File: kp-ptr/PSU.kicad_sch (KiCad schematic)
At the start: 34 parts, among them IC1 TPS62140ARGTR, J2 Conn_01x02, J3 Conn_01x02, U10 AZ1117CH-5.0TRG1, U9 LDFM33PVR

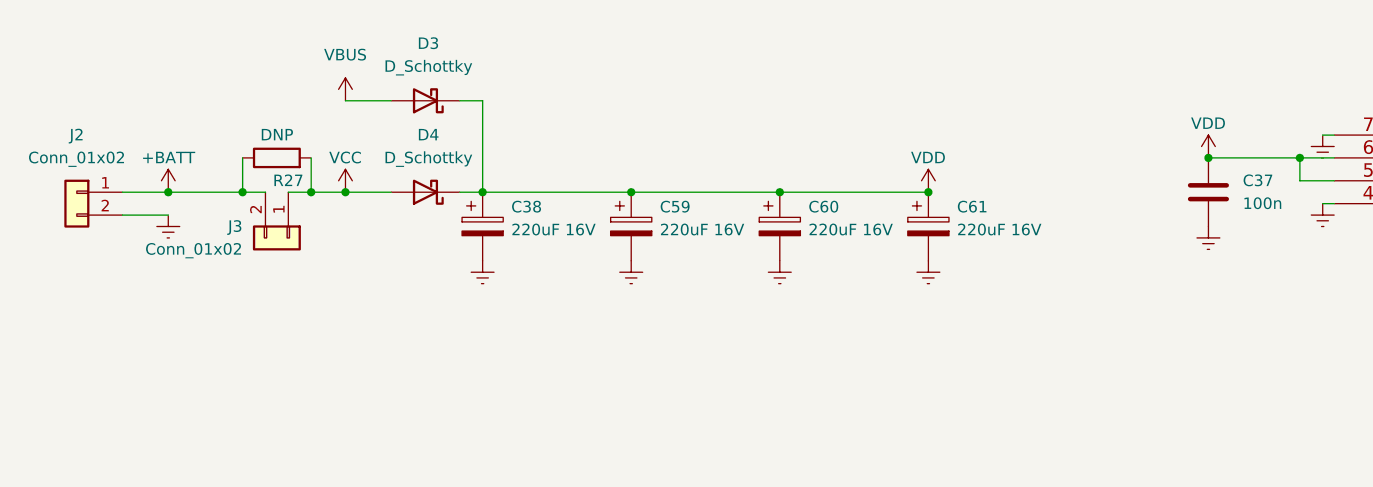
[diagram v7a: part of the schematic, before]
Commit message: SW removed, tantal added, powerplane rework
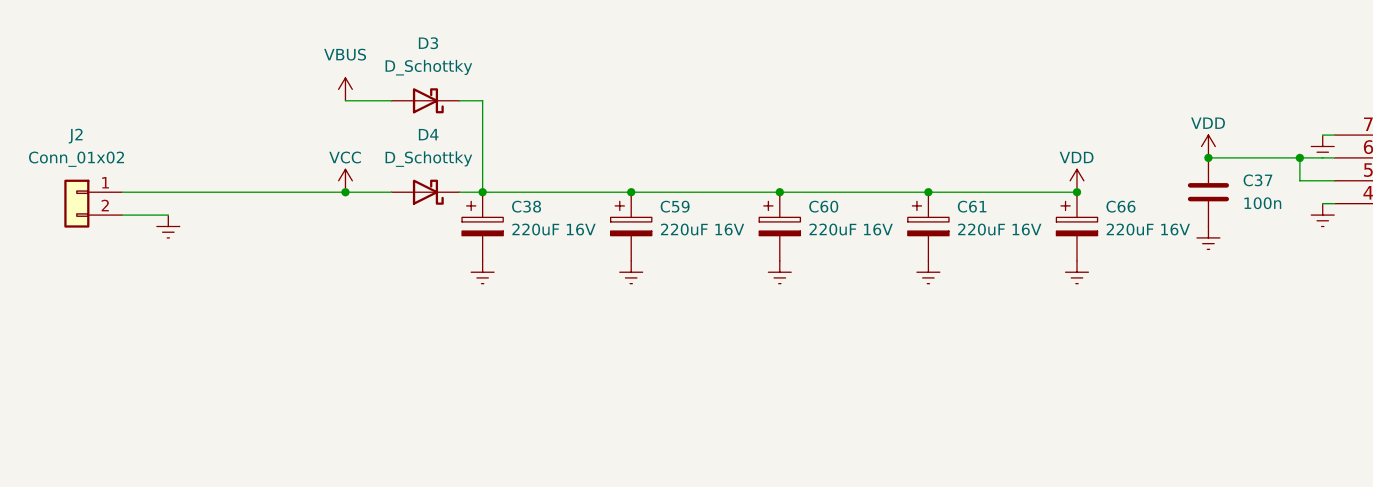
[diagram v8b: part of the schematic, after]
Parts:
- removed J3: Conn_01x02, TerminalBlock_TE-Connectivity:TerminalBlock_TE_282834-2_1x02_P2.54mm_Horizontal, symbol Connector_Generic:Conn_01x02
- removed R27: DNP, Resistor_SMD:R_1206_3216Metric, symbol Device:R
- added C66: 220uF 16V, Capacitor_Tantalum_SMD:CP_EIA-7343-31_Kemet-D, symbol Device:C_Polarized
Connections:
- net +BATT is gone; now on net VCC: J2.1 (Pin_1)
- net Earth: now also C66.2
- net VDD: now also C66.1
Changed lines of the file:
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@@
   (junction (at 41.275 97.79) (diameter 0) (color 0 0 0 0)
   )
-  (junction (at 47.625 44.45) (diameter 0) (color 0 0 0 0)
-  )
   (junction (at 149.86 129.54) (diameter 0) (color 0 0 0 0)
   )
@@
   (junction (at 147.32 40.64) (diameter 0) (color 0 0 0 0)
   )
-  (junction (at 31.75 44.45) (diameter 0) (color 0 0 0 0)
-  )
   (junction (at 137.16 132.08) (diameter 0) (color 0 0 0 0)
   )
   (junction (at 106.68 133.35) (diameter 0) (color 0 0 0 0)
   )
+  (junction (at 132.715 44.45) (diameter 0) (color 0 0 0 0)
+  )
   (junction (at 214.63 38.1) (diameter 0) (color 0 0 0 0)
-  )
-  (junction (at 40.005 44.45) (diameter 0) (color 0 0 0 0)
   )
   (junction (at 99.695 44.45) (diameter 0) (color 0 0 0 0)
@@
     (stroke (width 0) (type default) (color 0 0 0 0))
   )
-  (wire (pts (xy 45.085 44.45) (xy 47.625 44.45))
-    (stroke (width 0) (type default) (color 0 0 0 0))
-  )
   (wire (pts (xy 99.695 44.45) (xy 116.205 44.45))
     (stroke (width 0) (type default) (color 0 0 0 0))
@@
     (stroke (width 0) (type default) (color 0 0 0 0))
   )
-  (wire (pts (xy 47.625 40.64) (xy 47.625 44.45))
-    (stroke (width 0) (type default) (color 0 0 0 0))
-  )
   (wire (pts (xy 144.78 144.78) (xy 149.86 144.78))
     (stroke (width 0) (type default) (color 0 0 0 0))
@@
     (stroke (width 0) (type default) (color 0 0 0 0))
   )
-  (wire (pts (xy 47.625 44.45) (xy 51.435 44.45))
-    (stroke (width 0) (type default) (color 0 0 0 0))
-  )
-  (wire (pts (xy 26.67 44.45) (xy 31.75 44.45))
+  (wire (pts (xy 26.67 44.45) (xy 51.435 44.45))
+    (stroke (width 0) (type default) (color 0 0 0 0))
+  )
+  (wire (pts (xy 116.205 44.45) (xy 132.715 44.45))
     (stroke (width 0) (type default) (color 0 0 0 0))
   )
@@
     (stroke (width 0) (type default) (color 0 0 0 0))
   )
-  (wire (pts (xy 31.75 44.45) (xy 40.005 44.45))
-    (stroke (width 0) (type default) (color 0 0 0 0))
-  )
   (wire (pts (xy 160.02 38.1) (xy 161.29 38.1))
     (stroke (width 0) (type default) (color 0 0 0 0))
@@
     (stroke (width 0) (type default) (color 0 0 0 0))
   )
-  (wire (pts (xy 40.005 40.64) (xy 40.005 44.45))
-    (stroke (width 0) (type default) (color 0 0 0 0))
-  )
   (wire (pts (xy 149.86 129.54) (xy 155.575 129.54))
     (stroke (width 0) (type default) (color 0 0 0 0))
@@
   )
   (wire (pts (xy 137.16 132.08) (xy 137.16 134.62))
-    (stroke (width 0) (type default) (color 0 0 0 0))
-  )
-  (wire (pts (xy 40.005 44.45) (xy 42.545 44.45))
     (stroke (width 0) (type default) (color 0 0 0 0))
   )
@@
     (pin "1")
   )
+  (symbol (lib_id "power:Earth") (at 132.715 52.07 0) (unit 1)
+    (in_bom yes) (on_board yes) (fields_autoplaced)
+    (property "Reference" "#PWR098" (id 0) (at 132.715 58.42 0)
+      (effects (font (size 1.27 1.27)) hide)
+    )
+    (property "Value" "Earth" (id 1) (at 132.715 55.88 0)
+      (effects (font (size 1.27 1.27)) hide)
+    )
+    (property "Footprint" "" (id 2) (at 132.715 52.07 0)
+      (effects (font (size 1.27 1.27)) hide)
+    )
+    (property "Datasheet" "~" (id 3) (at 132.715 52.07 0)
+      (effects (font (size 1.27 1.27)) hide)
+    )
+    (pin "1")
+  )
   (symbol (lib_id "power:Earth") (at 106.68 157.48 0) (mirror y) (unit 1)
     (in_bom yes) (on_board yes) (fields_autoplaced)
@@
     )
     (property "Datasheet" "~" (id 3) (at 32.385 101.6 0)
-      (effects (font (size 1.27 1.27)) hide)
-    )
-    (pin "1")
-    (pin "2")
-  )
-  (symbol (lib_id "Device:R") (at 43.815 40.64 90) (unit 1)
-    (in_bom yes) (on_board yes)
-    (property "Reference" "R27" (id 0) (at 45.085 43.18 90))
-    (property "Value" "DNP" (id 1) (at 43.815 38.1 90))
-    (property "Footprint" "Resistor_SMD:R_1206_3216Metric" (id 2) (at 43.815 42.418 90)
-      (effects (font (size 1.27 1.27)) hide)
-    )
-    (property "Datasheet" "~" (id 3) (at 43.815 40.64 0)
       (effects (font (size 1.27 1.27)) hide)
     )
@@
     (pin "2")
   )
-  (symbol (lib_id "Connector_Generic:Conn_01x02") (at 45.085 49.53 270) (unit 1)
-    (in_bom yes) (on_board yes)
-    (property "Reference" "J3" (id 0) (at 40.005 48.2599 90)
-      (effects (font (size 1.27 1.27)) (justify right))
-    )
-    (property "Value" "Conn_01x02" (id 1) (at 40.005 50.7999 90)
-      (effects (font (size 1.27 1.27)) (justify right))
-    )
-    (property "Footprint" "TerminalBlock_TE-Connectivity:TerminalBlock_TE_282834-2_1x02_P2.54mm_Horizontal" (id 2) (at 45.085 49.53 0)
-      (effects (font (size 1.27 1.27)) hide)
-    )
-    (property "Datasheet" "~" (id 3) (at 45.085 49.53 0)
-      (effects (font (size 1.27 1.27)) hide)
-    )
-    (pin "1")
-    (pin "2")
-  )
   (symbol (lib_id "Device:C") (at 155.575 133.35 0) (mirror y) (unit 1)
     (in_bom yes) (on_board yes) (fields_autoplaced)
@@
     (pin "3")
     (pin "4")
-  )
-  (symbol (lib_id "power:+BATT") (at 31.75 44.45 0) (unit 1)
-    (in_bom yes) (on_board yes)
-    (property "Reference" "#PWR098" (id 0) (at 31.75 48.26 0)
-      (effects (font (size 1.27 1.27)) hide)
-    )
-    (property "Value" "+BATT" (id 1) (at 31.75 40.64 0))
-    (property "Footprint" "" (id 2) (at 31.75 44.45 0)
-      (effects (font (size 1.27 1.27)) hide)
-    )
-    (property "Datasheet" "" (id 3) (at 31.75 44.45 0)
-      (effects (font (size 1.27 1.27)) hide)
-    )
-    (pin "1")
   )
   (symbol (lib_id "KP-PTR_lib:TPS62140ARGTR") (at 121.92 144.78 0) (unit 1)
@@
     (pin "1")
   )
-  (symbol (lib_id "power:VDD") (at 116.205 44.45 0) (unit 1)
-    (in_bom yes) (on_board yes)
-    (property "Reference" "#PWR0100" (id 0) (at 116.205 48.26 0)
-      (effects (font (size 1.27 1.27)) hide)
-    )
-    (property "Value" "VDD" (id 1) (at 116.205 40.64 0))
-    (property "Footprint" "" (id 2) (at 116.205 44.45 0)
-      (effects (font (size 1.27 1.27)) hide)
-    )
-    (property "Datasheet" "" (id 3) (at 116.205 44.45 0)
+  (symbol (lib_id "power:VDD") (at 132.715 44.45 0) (unit 1)
+    (in_bom yes) (on_board yes)
+    (property "Reference" "#PWR0100" (id 0) (at 132.715 48.26 0)
+      (effects (font (size 1.27 1.27)) hide)
+    )
+    (property "Value" "VDD" (id 1) (at 132.715 40.64 0))
+    (property "Footprint" "" (id 2) (at 132.715 44.45 0)
+      (effects (font (size 1.27 1.27)) hide)
+    )
+    (property "Datasheet" "" (id 3) (at 132.715 44.45 0)
       (effects (font (size 1.27 1.27)) hide)
     )
@@
     (pin "1")
   )
+  (symbol (lib_id "Device:C_Polarized") (at 132.715 48.26 0) (unit 1)
+    (in_bom yes) (on_board yes) (fields_autoplaced)
+    (property "Reference" "C66" (id 0) (at 135.89 46.1009 0)
+      (effects (font (size 1.27 1.27)) (justify left))
+    )
+    (property "Value" "220uF 16V" (id 1) (at 135.89 48.6409 0)
+      (effects (font (size 1.27 1.27)) (justify left))
+    )
+    (property "Footprint" "Capacitor_Tantalum_SMD:CP_EIA-7343-31_Kemet-D" (id 2) (at 133.6802 52.07 0)
+      (effects (font (size 1.27 1.27)) hide)
+    )
+    (property "Datasheet" "~" (id 3) (at 132.715 48.26 0)
+      (effects (font (size 1.27 1.27)) hide)
+    )
+    (pin "1")
+    (pin "2")
+  )
   (symbol (lib_id "Device:C_Polarized") (at 116.205 48.26 0) (unit 1)
